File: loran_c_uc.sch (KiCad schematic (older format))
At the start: 37 parts, among them U701 STM32F407VG, X701 32.768KHz

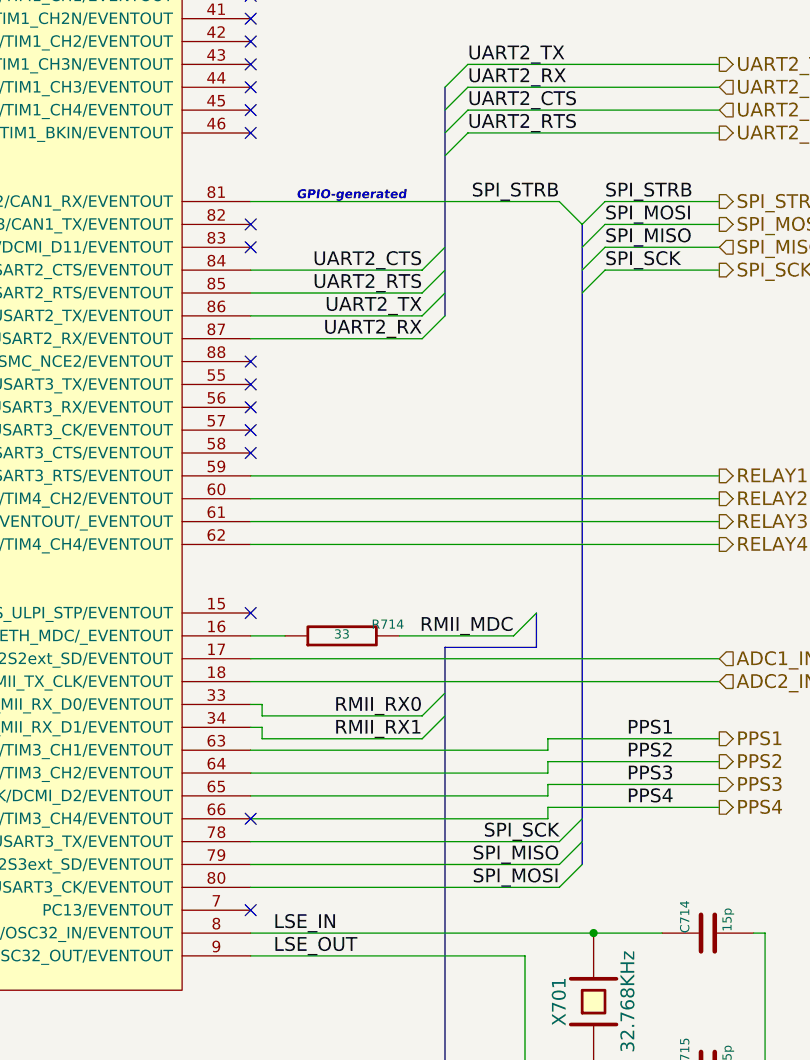
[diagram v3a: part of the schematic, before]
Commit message: Update: minor schematic rework (due to PCB routing), PCB routing in early stage
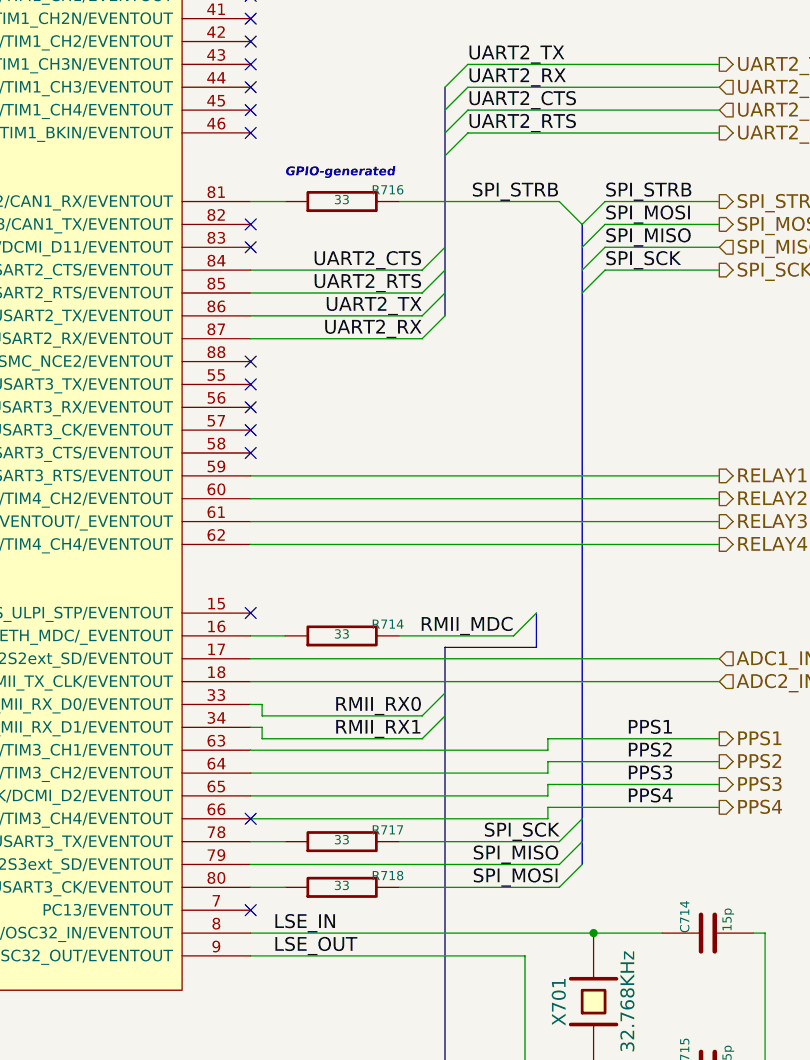
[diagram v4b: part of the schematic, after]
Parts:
- added R716, R717, R718: 33, w_smd_resistors:r_1206, symbol R
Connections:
- net SPI_MOSI: now also R718.2; no longer U701.80 (PC12/UART5_TX/SDIO_CK/DCMI_D9/SPI3_MOSI/I2S3_SD/USART3_CK/EVENTOUT)
- net SPI_SCK: now also R717.2; no longer U701.78 (PC10/SPI3_SCK/I2S3_CK/UART4_TX/SDIO_D2/DCMI_D8/USART3_TX/EVENTOUT)
- net SPI_STRB: now also R716.2; no longer U701.81 (PD0/FSMC_D2/CAN1_RX/EVENTOUT)
- new net: R717.1, U701.78 (PC10/SPI3_SCK/I2S3_CK/UART4_TX/SDIO_D2/DCMI_D8/USART3_TX/EVENTOUT)
- new net: R718.1, U701.80 (PC12/UART5_TX/SDIO_CK/DCMI_D9/SPI3_MOSI/I2S3_SD/USART3_CK/EVENTOUT)
- new net: R716.1, U701.81 (PD0/FSMC_D2/CAN1_RX/EVENTOUT)
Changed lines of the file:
@@
 $EndComp
 $Comp
-L AGND #PWR0126
+L AGND #PWR0127
 U 1 1 52D15FAD
 P 7950 8900
-F 0 "#PWR0126" H 7950 8900 40  0001 C CNN
+F 0 "#PWR0127" H 7950 8900 40  0001 C CNN
 F 1 "AGND" H 7950 8830 50  0000 C CNN
 F 2 "" H 7950 8900 60  0000 C CNN
@@
 $EndComp
 $Comp
-L GND #PWR0127
+L GND #PWR0128
 U 1 1 52D16322
 P 8150 8900
-F 0 "#PWR0127" H 8150 8900 30  0001 C CNN
+F 0 "#PWR0128" H 8150 8900 30  0001 C CNN
 F 1 "GND" H 8150 8830 30  0001 C CNN
 F 2 "" H 8150 8900 60  0000 C CNN
@@
 $EndComp
 $Comp
-L GND #PWR0128
+L GND #PWR0129
 U 1 1 52D16334
 P 8350 8900
-F 0 "#PWR0128" H 8350 8900 30  0001 C CNN
+F 0 "#PWR0129" H 8350 8900 30  0001 C CNN
 F 1 "GND" H 8350 8830 30  0001 C CNN
 F 2 "" H 8350 8900 60  0000 C CNN
@@
 $EndComp
 $Comp
-L GND #PWR0129
+L GND #PWR0130
 U 1 1 52D16344
 P 8550 8900
-F 0 "#PWR0129" H 8550 8900 30  0001 C CNN
+F 0 "#PWR0130" H 8550 8900 30  0001 C CNN
 F 1 "GND" H 8550 8830 30  0001 C CNN
 F 2 "" H 8550 8900 60  0000 C CNN
@@
 $EndComp
 $Comp
-L GND #PWR0130
+L GND #PWR0131
 U 1 1 52D16354
 P 8750 8900
-F 0 "#PWR0130" H 8750 8900 30  0001 C CNN
+F 0 "#PWR0131" H 8750 8900 30  0001 C CNN
 F 1 "GND" H 8750 8830 30  0001 C CNN
 F 2 "" H 8750 8900 60  0000 C CNN
@@
 $EndComp
 $Comp
-L GND #PWR0131
+L GND #PWR0132
 U 1 1 52D16366
 P 9250 8900
-F 0 "#PWR0131" H 9250 8900 30  0001 C CNN
+F 0 "#PWR0132" H 9250 8900 30  0001 C CNN
 F 1 "GND" H 9250 8830 30  0001 C CNN
 F 2 "" H 9250 8900 60  0000 C CNN
@@
 $EndComp
 $Comp
-L GND #PWR0132
+L GND #PWR0133
 U 1 1 52D16378
 P 9750 8900
-F 0 "#PWR0132" H 9750 8900 30  0001 C CNN
+F 0 "#PWR0133" H 9750 8900 30  0001 C CNN
 F 1 "GND" H 9750 8830 30  0001 C CNN
 F 2 "" H 9750 8900 60  0000 C CNN
@@
 $EndComp
 $Comp
-L GND #PWR0133
+L GND #PWR0134
 U 1 1 52D1638A
 P 7600 1600
-F 0 "#PWR0133" H 7600 1600 30  0001 C CNN
+F 0 "#PWR0134" H 7600 1600 30  0001 C CNN
 F 1 "GND" H 7600 1530 30  0001 C CNN
 F 2 "" H 7600 1600 60  0000 C CNN
@@
 $EndComp
 $Comp
-L GND #PWR0134
+L GND #PWR0135
 U 1 1 52D1639C
 P 7900 1600
-F 0 "#PWR0134" H 7900 1600 30  0001 C CNN
+F 0 "#PWR0135" H 7900 1600 30  0001 C CNN
 F 1 "GND" H 7900 1530 30  0001 C CNN
 F 2 "" H 7900 1600 60  0000 C CNN
@@
 $EndComp
 $Comp
-L GND #PWR0135
+L GND #PWR0136
 U 1 1 52D163AC
 P 8200 1600
-F 0 "#PWR0135" H 8200 1600 30  0001 C CNN
+F 0 "#PWR0136" H 8200 1600 30  0001 C CNN
 F 1 "GND" H 8200 1530 30  0001 C CNN
 F 2 "" H 8200 1600 60  0000 C CNN
@@
 $EndComp
 $Comp
-L GND #PWR0136
+L GND #PWR0137
 U 1 1 52D163BC
 P 8500 1600
-F 0 "#PWR0136" H 8500 1600 30  0001 C CNN
+F 0 "#PWR0137" H 8500 1600 30  0001 C CNN
 F 1 "GND" H 8500 1530 30  0001 C CNN
 F 2 "" H 8500 1600 60  0000 C CNN
@@
 $EndComp
 $Comp
-L GND #PWR0137
+L GND #PWR0138
 U 1 1 52D163CC
 P 8800 1600
-F 0 "#PWR0137" H 8800 1600 30  0001 C CNN
+F 0 "#PWR0138" H 8800 1600 30  0001 C CNN
 F 1 "GND" H 8800 1530 30  0001 C CNN
 F 2 "" H 8800 1600 60  0000 C CNN
@@
 $EndComp
 $Comp
-L GND #PWR0138
+L GND #PWR0139
 U 1 1 52D163DC
 P 9100 1600
-F 0 "#PWR0138" H 9100 1600 30  0001 C CNN
+F 0 "#PWR0139" H 9100 1600 30  0001 C CNN
 F 1 "GND" H 9100 1530 30  0001 C CNN
 F 2 "" H 9100 1600 60  0000 C CNN
@@
 $EndComp
 $Comp
-L VDD #PWR0139
+L VDD #PWR0140
 U 1 1 52D16440
 P 7900 800
-F 0 "#PWR0139" H 7900 900 30  0001 C CNN
+F 0 "#PWR0140" H 7900 900 30  0001 C CNN
 F 1 "VDD" H 7900 910 30  0000 C CNN
 F 2 "" H 7900 800 60  0000 C CNN
@@
 $EndComp
 $Comp
-L +3.3VADC #PWR0140
+L +3.3VADC #PWR0141
 U 1 1 52D26AB8
 P 6600 800
-F 0 "#PWR0140" H 6600 920 20  0001 C CNN
+F 0 "#PWR0141" H 6600 920 20  0001 C CNN
 F 1 "+3.3VADC" H 6600 890 30  0000 C CNN
 F 2 "" H 6600 800 60  0000 C CNN
@@
 $EndComp
 $Comp
-L AGND #PWR0141
+L AGND #PWR0142
 U 1 1 52D26ACC
 P 5000 1550
-F 0 "#PWR0141" H 5000 1550 40  0001 C CNN
+F 0 "#PWR0142" H 5000 1550 40  0001 C CNN
 F 1 "AGND" H 5000 1480 50  0000 C CNN
 F 2 "" H 5000 1550 60  0000 C CNN
@@
 $EndComp
 $Comp
-L AGND #PWR0142
+L AGND #PWR0143
 U 1 1 52D26ADE
 P 5400 1550
-F 0 "#PWR0142" H 5400 1550 40  0001 C CNN
+F 0 "#PWR0143" H 5400 1550 40  0001 C CNN
 F 1 "AGND" H 5400 1480 50  0000 C CNN
 F 2 "" H 5400 1550 60  0000 C CNN
@@
 $EndComp
 $Comp
-L AGND #PWR0143
+L AGND #PWR0144
 U 1 1 52D26AE9
 P 5400 2200
-F 0 "#PWR0143" H 5400 2200 40  0001 C CNN
+F 0 "#PWR0144" H 5400 2200 40  0001 C CNN
 F 1 "AGND" H 5400 2130 50  0000 C CNN
 F 2 "" H 5400 2200 60  0000 C CNN
@@
 $EndComp
 $Comp
-L AGND #PWR0144
+L AGND #PWR0145
 U 1 1 52D26AF4
 P 5000 2200
-F 0 "#PWR0144" H 5000 2200 40  0001 C CNN
+F 0 "#PWR0145" H 5000 2200 40  0001 C CNN
 F 1 "AGND" H 5000 2130 50  0000 C CNN
 F 2 "" H 5000 2200 60  0000 C CNN
@@
 $EndComp
 $Comp
-L VDD #PWR0145
+L VDD #PWR0146
 U 1 1 52D26E0C
 P 1250 1350
-F 0 "#PWR0145" H 1250 1450 30  0001 C CNN
+F 0 "#PWR0146" H 1250 1450 30  0001 C CNN
 F 1 "VDD" H 1250 1460 30  0000 C CNN
 F 2 "" H 1250 1350 60  0000 C CNN
@@
 $EndComp
 $Comp
-L GND #PWR0146
+L GND #PWR0147
 U 1 1 52D27009
 P 2050 2000
-F 0 "#PWR0146" H 2050 2000 30  0001 C CNN
+F 0 "#PWR0147" H 2050 2000 30  0001 C CNN
 F 1 "GND" H 2050 1930 30  0001 C CNN
 F 2 "" H 2050 2000 60  0000 C CNN
@@
 $EndComp
 $Comp
-L GND #PWR0147
+L GND #PWR0148
 U 1 1 52D2779C
 P 1750 6500
-F 0 "#PWR0147" H 1750 6500 30  0001 C CNN
+F 0 "#PWR0148" H 1750 6500 30  0001 C CNN
 F 1 "GND" H 1750 6430 30  0001 C CNN
 F 2 "" H 1750 6500 60  0000 C CNN
@@
 $EndComp
 $Comp
-L GND #PWR0148
+L GND #PWR0149
 U 1 1 52D28928
 P 15600 8450
-F 0 "#PWR0148" H 15600 8450 30  0001 C CNN
+F 0 "#PWR0149" H 15600 8450 30  0001 C CNN
 F 1 "GND" H 15600 8380 30  0001 C CNN
 F 2 "" H 15600 8450 60  0000 C CNN
@@
 $EndComp
 $Comp
-L GND #PWR0149
+L GND #PWR0150
 U 1 1 52D31B27
 P 3000 8400
-F 0 "#PWR0149" H 3000 8400 30  0001 C CNN
+F 0 "#PWR0150" H 3000 8400 30  0001 C CNN
 F 1 "GND" H 3000 8330 30  0001 C CNN
 F 2 "" H 3000 8400 60  0000 C CNN
@@
 $EndComp
 $Comp
-L GND #PWR0150
+L GND #PWR0151
 U 1 1 52D31DF9
 P 3250 8400
-F 0 "#PWR0150" H 3250 8400 30  0001 C CNN
+F 0 "#PWR0151" H 3250 8400 30  0001 C CNN
 F 1 "GND" H 3250 8330 30  0001 C CNN
 F 2 "" H 3250 8400 60  0000 C CNN
@@
 $EndComp
 $Comp
-L GND #PWR0151
+L GND #PWR0152
 U 1 1 52D3210D
 P 1750 6300
-F 0 "#PWR0151" H 1750 6300 30  0001 C CNN
+F 0 "#PWR0152" H 1750 6300 30  0001 C CNN
 F 1 "GND" H 1750 6230 30  0001 C CNN
 F 2 "" H 1750 6300 60  0000 C CNN
@@
 $EndComp
 $Comp
-L GND #PWR0152
+L GND #PWR0153
 U 1 1 52D32123
 P 1750 6100
-F 0 "#PWR0152" H 1750 6100 30  0001 C CNN
+F 0 "#PWR0153" H 1750 6100 30  0001 C CNN
 F 1 "GND" H 1750 6030 30  0001 C CNN
 F 2 "" H 1750 6100 60  0000 C CNN
@@
 $EndComp
 $Comp
-L GND #PWR0153
+L GND #PWR0154
 U 1 1 52D5BFEE
 P 3200 4500
-F 0 "#PWR0153" H 3200 4500 30  0001 C CNN
+F 0 "#PWR0154" H 3200 4500 30  0001 C CNN
 F 1 "GND" H 3200 4430 30  0001 C CNN
 F 2 "" H 3200 4500 60  0000 C CNN
@@
 Text Notes 1700 7300 0    39   Italic 8
 GPIO-generated
-Text Notes 13550 4500 0    39   Italic 8
+Text Notes 13500 4400 0    39   Italic 8
 GPIO-generated
 $Comp
@@
 $EndComp
 $Comp
-L GND #PWR0154
+L GND #PWR0155
 U 1 1 52E12477
 P 2050 2700
-F 0 "#PWR0154" H 2050 2700 30  0001 C CNN
+F 0 "#PWR0155" H 2050 2700 30  0001 C CNN
 F 1 "GND" H 2050 2630 30  0001 C CNN
 F 2 "" H 2050 2700 60  0000 C CNN
@@
 $EndComp
 $Comp
-L GND #PWR0155
+L GND #PWR0156
 U 1 1 52E12CEB
 P 1250 2700
-F 0 "#PWR0155" H 1250 2700 30  0001 C CNN
+F 0 "#PWR0156" H 1250 2700 30  0001 C CNN
 F 1 "GND" H 1250 2630 30  0001 C CNN
 F 2 "" H 1250 2700 60  0000 C CNN
@@
 	14650 6950 15400 6950
 Wire Wire Line
-	13350 4500 14700 4500
+	13350 4500 13500 4500
+Wire Wire Line
+	14000 4500 14700 4500
 Wire Bus Line
 	14800 4600 14800 7400
@@
 	2900 6600 3350 6600
 Wire Wire Line
-	13350 7500 14700 7500
-Wire Wire Line
-	14700 7400 13350 7400
-Wire Wire Line
-	13350 7300 14700 7300
+	13350 7500 13500 7500
+Wire Wire Line
+	14000 7500 14700 7500
+Wire Wire Line
+	13350 7400 14700 7400
+Wire Wire Line
+	13350 7300 13500 7300
+Wire Wire Line
+	14000 7300 14700 7300
 Wire Wire Line
 	14100 5100 13350 5100
@@
 NoConn ~ 3350 6600
 NoConn ~ 3350 6700
+$Comp
+L R R718
+U 1 1 52E6300A
+P 13750 7500
+F 0 "R718" V 13800 7300 40  0000 C CNN
+F 1 "33" V 13757 7501 40  0000 C CNN
+F 2 "w_smd_resistors:r_1206" V 13680 7500 30  0001 C CNN
+F 3 "" H 13750 7500 30  0000 C CNN
+	1    13750 7500
+	0    -1   -1   0
+$EndComp
+$Comp
+L R R717
+U 1 1 52E635AA
+P 13750 7300
+F 0 "R717" V 13800 7100 40  0000 C CNN
+F 1 "33" V 13757 7301 40  0000 C CNN
+F 2 "w_smd_resistors:r_1206" V 13680 7300 30  0001 C CNN
+F 3 "" H 13750 7300 30  0000 C CNN
+	1    13750 7300
+	0    -1   -1   0
+$EndComp
+$Comp
+L R R716
+U 1 1 52E635B5
+P 13750 4500
+F 0 "R716" V 13800 4300 40  0000 C CNN
+F 1 "33" V 13757 4501 40  0000 C CNN
+F 2 "w_smd_resistors:r_1206" V 13680 4500 30  0001 C CNN
+F 3 "" H 13750 4500 30  0000 C CNN
+	1    13750 4500
+	0    -1   -1   0
+$EndComp
 $EndSCHEMATC

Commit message: Intermediate update #2: PCB routing/schematic tweaking in process
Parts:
- removed R705, R714: 33, w_smd_resistors:r_1206, symbol R
- added C716: 100n, w_smd_capacitors:c_1206, symbol C
- added R719: 33, w_smd_resistors:r_1206, symbol R
- added R720: 1.5k, w_smd_resistors:r_1206, symbol R
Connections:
- net JTAG_NRST is gone; now on net SPI_MISO: U701.90 (PB4/NJTRST/SPI3_MISO/TIM3_CH1/SPI1_MISO/I2S3ext_SD/EVENTOUT)
- net GND: now also C716.2; no longer U701.23 (PA0/WKUP/USART2_CTS/UART4_TX/ETH_MII_CRS_/TIM2_CH1_ETR/TIM5_CH1/TIM8_ETR/EVENTOUT)
- net LSE_IN: now also X701.1; no longer X701.2
- net LSE_OUT: now also X701.2; no longer X701.1
- net RMII_MDC: now also U701.16 (PC1/ETH_MDC/_EVENTOUT)
- net RMII_MDIO: now also U701.25 (PA2/USART2_TX/TIM5_CH3/TIM9_CH1/TIM2_CH3/ETH_MDIO/EVENTOUT), R720.1
- net RMII_NRST: now also R719.1; no longer U701.47 (PB10/SPI2_SCK/I2S2_CK/I2C2_SCL/USART3_TX/OTG_HS_ULPI_D3/ETH_MII_RX_ER/TIM2_CH3/EVENTOUT)
- net SPI_MISO: no longer U701.79 (PC11/UART4_RX/SPI3_MISO/SDIO_D3/DCMI_D4/USART3_RX/I2S3ext_SD/EVENTOUT)
- net SPI_MOSI: now also R718.1; no longer R718.2
- net SPI_SCK: now also R717.1; no longer R717.2
- net SPI_STRB: now also R716.1; no longer R716.2
- net VDD: now also C716.1, R720.2
- net at U701.78 (PC10/SPI3_SCK/I2S3_CK/UART4_TX/SDIO_D2/DCMI_D8/USART3_TX/EVENTOUT): no longer R717.1
- net at U701.80 (PC12/UART5_TX/SDIO_CK/DCMI_D9/SPI3_MOSI/I2S3_SD/USART3_CK/EVENTOUT): no longer R718.1
- net at U701.81 (PD0/FSMC_D2/CAN1_RX/EVENTOUT): no longer R716.1
- net at R712.1, U701.91 (PB5/I2C1_SMBA/CAN2_RX/OTG_HS_ULPI_D7/ETH_PPS_OUT/TIM3_CH2/SPI1_MOSI/SPI3_MOSI/DCMI_D10/I2S3_SD/EVENTOUT): now also R718.2
- net at U701.92 (PB6/I2C1_SCL/TIM4_CH1/CAN2_TX/DCMI_D5/USART1_TX/EVENTOUT): now also R716.2
- net JTAG_TDO: no longer names the net of U701.89 (PB3/JTDO/TRACESWO/SPI3_SCK/I2S3_CK/TIM2_CH2/SPI1_SCK/EVENTOUT)
- net JTAG_TDO: now also R717.2
- new net: R719.2, U701.47 (PB10/SPI2_SCK/I2S2_CK/I2C2_SCL/USART3_TX/OTG_HS_ULPI_D3/ETH_MII_RX_ER/TIM2_CH3/EVENTOUT)
- no-connect marks 39 -> 40
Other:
- note added: "RMII MDIO/MDC lines: no termination resistors (on uC side),\nbecause interface (SMI) is deliberately down-clocked,\nslew rate controllably decreased via GPIOx_OSPEEDR\nto reduce ringing"
- moved on the sheet: R701, R702, R703, R716, R717, R718

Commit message: Update: lots of refactoring and pin remap ..In chase for easier PCB routing PCB still not completed
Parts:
- removed R709, R710: 33, w_smd_resistors:r_1206, symbol R
- added R705: 3.3k, w_smd_resistors:r_1206, symbol R
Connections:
- net PPS4 is gone; now on net PPS1: U701.66 (PC9/I2S_CKIN/MCO2/TIM8_CH4/SDIO_D1/I2C3_SDA/DCMI_D3/TIM3_CH4/EVENTOUT)
- net PPS1: no longer U701.63 (PC6/I2S2_MCK/TIM8_CH1/SDIO_D6/USART6_TX/DCMI_D0/TIM3_CH1/EVENTOUT)
- net PPS2: now also U701.65 (PC8/TIM8_CH3/SDIO_D0/TIM3_CH3/USART6_CK/DCMI_D2/EVENTOUT); no longer U701.64 (PC7/I2S3_MCK/TIM8_CH2/SDIO_D7/USART6_RX/DCMI_D1/TIM3_CH2/EVENTOUT)
- net PPS3: now also U701.93 (PB7/I2C1_SDA/FSMC_NL/DCMI_VSYNC/USART1_RX/TIM4_CH2/EVENTOUT); no longer U701.65 (PC8/TIM8_CH3/SDIO_D0/TIM3_CH3/USART6_CK/DCMI_D2/EVENTOUT)
- net VDD: now also R705.2
- net at C701.1, D701.1 (A), JP702.2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: now also R705.1
- net ADC3_IN: now reaches U701.15 (PC0/OTG_HS_ULPI_STP/EVENTOUT)
- net PPS_IN: now reaches U701.95 (PB8/TIM4_CH3/SDIO_D4/TIM10_CH1/DCMI_D6/ETH_MII_TXD3/I2C1_SCL/CAN1_RX/EVENTOUT)
- no-connect marks 40 -> 41

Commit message: Update: PCB routing still in process...
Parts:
- removed R719: 33, w_smd_resistors:r_1206, symbol R
- removed X701: 32.768KHz, symbol CRYSTAL
- added X701: 32.768KHz, symbol CRYSTAL_SHIELDED
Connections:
- net GND: now also X701.3
- net LSE_IN: now also X701.2
- net LSE_OUT: now also X701.1
- net PPS3: now also U701.95 (PB8/TIM4_CH3/SDIO_D4/TIM10_CH1/DCMI_D6/ETH_MII_TXD3/I2C1_SCL/CAN1_RX/EVENTOUT); no longer U701.93 (PB7/I2C1_SDA/FSMC_NL/DCMI_VSYNC/USART1_RX/TIM4_CH2/EVENTOUT)
- net PPS_IN: now also U701.93 (PB7/I2C1_SDA/FSMC_NL/DCMI_VSYNC/USART1_RX/TIM4_CH2/EVENTOUT); no longer U701.95 (PB8/TIM4_CH3/SDIO_D4/TIM10_CH1/DCMI_D6/ETH_MII_TXD3/I2C1_SCL/CAN1_RX/EVENTOUT)
- net RELAY1: now also U701.41 (PE10/FSMC_D7/TIM1_CH2N/EVENTOUT); no longer U701.59 (PD12/FSMC_ALE/FSMC_A17/TIM4_CH1/USART3_RTS/EVENTOUT)
- net RELAY2: now also U701.42 (PE11/FSMC_D8/TIM1_CH2/EVENTOUT); no longer U701.60 (PD13/FSMC_A18/TIM4_CH2/EVENTOUT)
- net RELAY3: now also U701.43 (PE12/FSMC_D9/TIM1_CH3N/EVENTOUT); no longer U701.61 (PD14/FSMC_D0/TIM4_CH3/EVENTOUT/_EVENTOUT)
- net RELAY4: now also U701.44 (PE13/FSMC_D10/TIM1_CH3/EVENTOUT); no longer U701.62 (PD15/FSMC_D1/TIM4_CH4/EVENTOUT)
- net RMII_NRST: now also U701.47 (PB10/SPI2_SCK/I2S2_CK/I2C2_SCL/USART3_TX/OTG_HS_ULPI_D3/ETH_MII_RX_ER/TIM2_CH3/EVENTOUT)
- net RMII_TX_EN: now also R711.1
- net SPI_MOSI: now also R712.1
- net at R706.2, U701.48 (PB11/I2C2_SDA/USART3_RX/OTG_HS_ULPI_D4/ETH_RMII_TX_EN/ETH_MII_TX_EN/TIM2_CH4/EVENTOUT): no longer R711.1
- net at R718.2, U701.91 (PB5/I2C1_SMBA/CAN2_RX/OTG_HS_ULPI_D7/ETH_PPS_OUT/TIM3_CH2/SPI1_MOSI/SPI3_MOSI/DCMI_D10/I2S3_SD/EVENTOUT): no longer R712.1
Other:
- moved on the sheet: R706, R707, R708, R711, R712
